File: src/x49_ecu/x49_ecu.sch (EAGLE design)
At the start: 20 parts, among them J1 1-776163-4, J2 DTP13-4P, J3 DTP13-4P

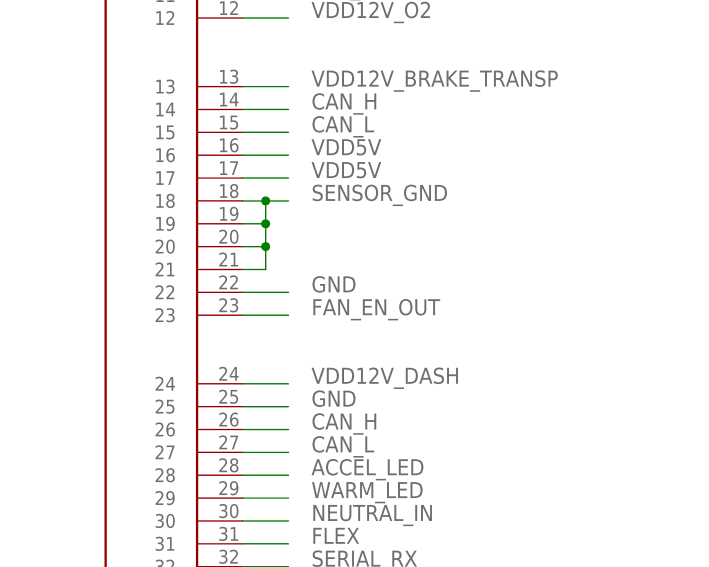
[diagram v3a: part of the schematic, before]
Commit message: x49_ecu: Rev 1E with fixed O2 sensor gnd
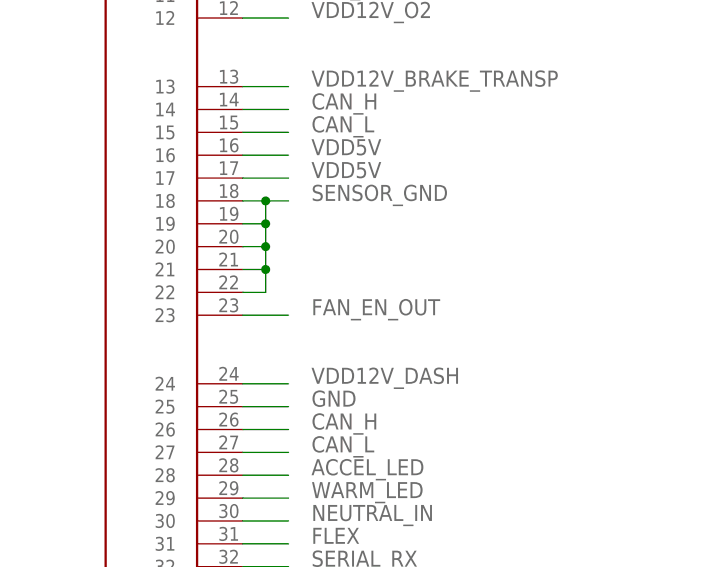
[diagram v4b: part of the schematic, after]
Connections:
- net GND: no longer J1.22
- net SENSOR_GND: now also J1.22
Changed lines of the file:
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@@
 <?xml version="1.0" encoding="utf-8"?>
 <!DOCTYPE eagle SYSTEM "eagle.dtd">
-<eagle version="9.3.0">
+<eagle version="9.3.1">
 <drawing>
 <settings>
@@
 </segment>
 <segment>
-<pinref part="J1" gate="G$1" pin="22"/>
-<wire x1="20.32" y1="43.18" x2="25.4" y2="43.18" width="0.1524" layer="91"/>
-<label x="27.94" y="43.18" size="1.778" layer="95"/>
-</segment>
-<segment>
 <pinref part="J3" gate="G$1" pin="3"/>
 <wire x1="20.32" y1="-60.96" x2="22.86" y2="-60.96" width="0.1524" layer="91"/>
@@
 <wire x1="22.86" y1="48.26" x2="22.86" y2="45.72" width="0.1524" layer="91"/>
 <junction x="22.86" y="48.26"/>
-</segment>
-</net>
+<pinref part="J1" gate="G$1" pin="22"/>
+<wire x1="20.32" y1="43.18" x2="22.86" y2="43.18" width="0.1524" layer="91"/>
+<wire x1="22.86" y1="43.18" x2="22.86" y2="45.72" width="0.1524" layer="91"/>
+<junction x="22.86" y="45.72"/>
+</segment>
+</net>
